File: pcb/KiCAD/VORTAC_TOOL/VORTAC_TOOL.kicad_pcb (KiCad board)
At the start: 4 copper layers, 18.2 x 7.6 mm, 6 parts, among them J1 Conn_01x05, J2 Conn_01x02, J3 Conn_01x03

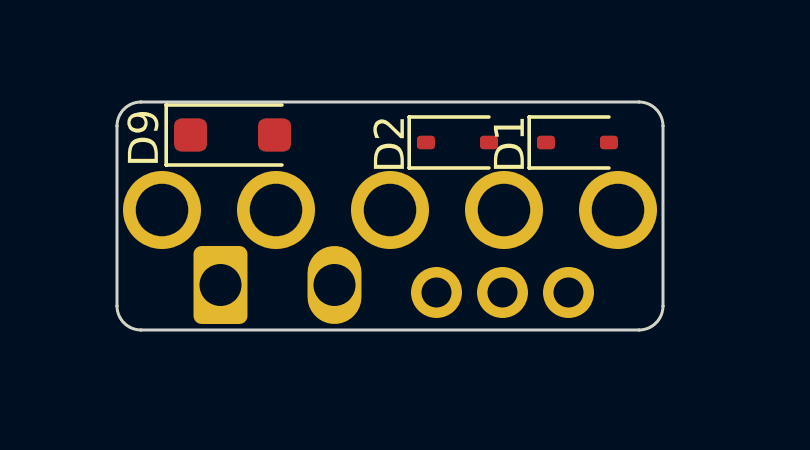
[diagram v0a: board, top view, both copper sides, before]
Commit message: updateting Custom Foorprints to show Ref**
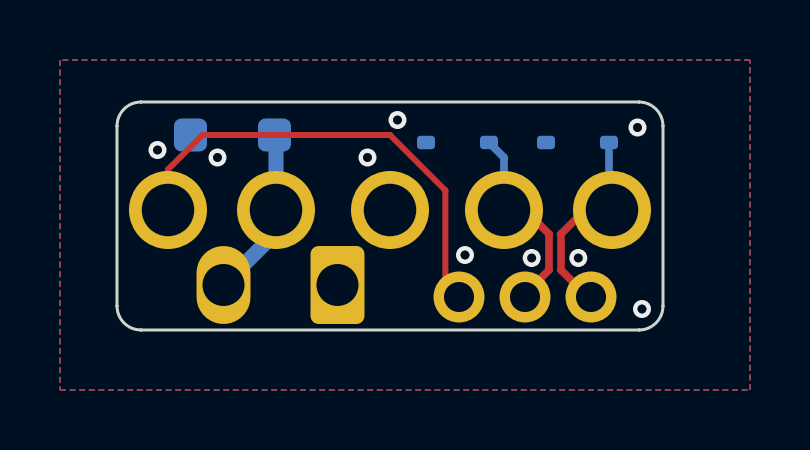
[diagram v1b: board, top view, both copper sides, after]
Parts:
- D1, D2, J1, J2, J3: moved to B.Cu
- D3: renamed from D9; moved to B.Cu
- moved J1 7.60 mm to (101.0, 52.0), turned to 0 degrees
- moved J2 3.90 mm to (99.2, 54.5)
- moved J3 0.76 mm to (103.3, 54.9), turned to -90 degrees
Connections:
- J1 pad 1: VDC -> TOOL_ID
- J1 pad 2: TOOL_ID -> VDC
- J1 pad 4: CAN_H -> CAN_L
- J1 pad 5: CAN_L -> CAN_H
- J3 pad 2: CAN_H -> CAN_L
- J3 pad 3: CAN_L -> CAN_H
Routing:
- net TOOL_ID: track 0.00 -> 15.5 mm
- net CAN_H: track 0.00 -> 6.80 mm
- net CAN_L: track 0.00 -> 6.76 mm
- net VDC: track 0.00 -> 5.75 mm
- net GND: track 0.00 -> 0.75 mm, vias 0 -> 9
- added copper zone on B.Cu, net GND
- added copper zone on F.Cu, net GND
- added copper zone on In1.Cu, net VDC
- added copper zone on In2.Cu, net VDC

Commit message: Added VORTAC_TOOLPLATE_REV2
Modified VORTAC_TOOL
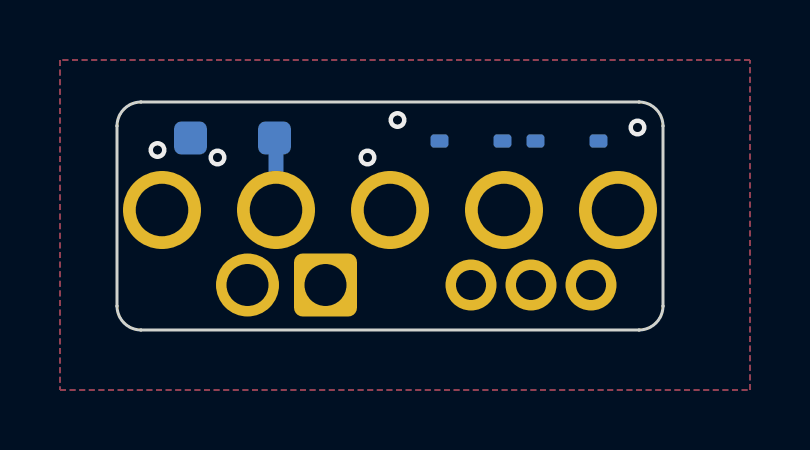
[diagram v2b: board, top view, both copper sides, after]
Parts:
- J3: footprint Vortac:Toolplate_Solderpoint_01x03_Data -> Vortac:Toolplate_Solderpoint_01x03_Data_Small
- moved J3 0.57 mm to (103.7, 54.5)
- moved D2 0.45 mm to (103.7, 49.7)
- moved J2 0.40 mm to (98.8, 54.5)
- moved D1 0.35 mm to (106.9, 49.7)
- moved D3 0.10 mm to (95.8, 49.6)
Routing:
- net TOOL_ID: track 15.5 -> 0.00 mm
- net CAN_H: track 6.80 -> 0.00 mm
- net CAN_L: track 6.76 -> 0.00 mm
- net VDC: track 5.75 -> 2.52 mm
- net GND: track 0.75 -> 0.00 mm, vias 9 -> 5
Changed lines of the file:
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@@
 	(footprint "Vortac:Toolplate_Solderpoint_01x02_Power_Small"
 		(layer "B.Cu")
-		(at 99.25 54.5 90)
+		(at 98.85 54.5 90)
 		(property "Reference" "J2"
 			(at 0 2.6 270)
@@
 		)
 		(pad "1" thru_hole roundrect
-			(at 0 0 90)
-			(size 2.6 1.8)
+			(at 0 0)
+			(size 2.1 2.1)
 			(drill 1.4)
 			(layers "*.Cu" "*.Mask")
 			(remove_unused_layers no)
-			(roundrect_rratio 0.15)
+			(roundrect_rratio 0.1388888889)
 			(net 3 "GND")
 			(pinfunction "Pin_1")
@@
 			(thermal_bridge_angle 0)
 		)
-		(pad "2" thru_hole oval
-			(at 0 -3.8 90)
-			(size 2.6 1.8)
+		(pad "2" thru_hole circle
+			(at 0 -2.6)
+			(size 2.1 2.1)
 			(drill 1.4)
 			(layers "*.Cu" "*.Mask")
@@
 		)
 		(pad "1" thru_hole circle
-			(at -7.4 0)
+			(at -7.6 0)
 			(size 2.6 2.6)
 			(drill 1.75)
@@
 		)
 		(pad "5" thru_hole circle
-			(at 7.4 0)
+			(at 7.6 0)
 			(size 2.6 2.6)
 			(drill 1.75)
@@
 		(embedded_fonts no)
 	)
-	(footprint "Vortac:Toolplate_Solderpoint_01x03_Data"
+	(footprint "Vortac:Toolplate_Solderpoint_01x03_Data_Small"
 		(layer "B.Cu")
-		(at 103.3 54.9 -90)
+		(at 103.7 54.5 -90)
 		(property "Reference" "J3"
 			(at 0.04 1.75 90)
@@
 		(attr smd exclude_from_bom)
 		(fp_text user "${REFERENCE}"
-			(at 0.25 -6.2 0)
+			(at -3.2 -2.6 0)
 			(unlocked yes)
 			(layer "B.Fab")
@@
 		)
 		(pad "2" thru_hole circle
-			(at 0 -2.2 270)
+			(at 0 -2 270)
 			(size 1.7 1.7)
 			(drill 1)
@@
 		)
 		(pad "3" thru_hole circle
-			(at 0 -4.4 270)
+			(at 0 -4 270)
 			(size 1.7 1.7)
 			(drill 1)
@@
 	(footprint "Diode_SMD:D_SOD-323"
 		(layer "B.Cu")
-		(at 103.25 49.75)
+		(at 103.7 49.7)
 		(descr "SOD-323")
 		(tags "SOD-323")
@@
 			(at -2.25 -0.05 90)
 			(layer "B.SilkS")
+			(hide yes)
 			(effects
 				(font
@@
 			(at 0.1 -1.9 180)
 			(layer "B.Fab")
+			(hide yes)
 			(effects
 				(font
@@
 	(footprint "Diode_SMD:D_SOD-123F"
 		(layer "B.Cu")
-		(at 95.75 49.5)
+		(at 95.75 49.6)
 		(descr "D_SOD-123F")
 		(tags "D_SOD-123F")
@@
 			(at -2.95 -0.1 90)
 			(layer "B.SilkS")
+			(hide yes)
 			(effects
 				(font
@@
 		)
 		(property "Value" "PTVS26VS1UR,115-ES"
-			(at 5.7 -3.5 180)
-			(layer "B.Fab")
+			(at 0.45 -3.55 180)
+			(layer "B.Fab")
+			(hide yes)
 			(effects
 				(font
@@
 	(footprint "Diode_SMD:D_SOD-323"
 		(layer "B.Cu")
-		(at 107.25 49.75)
+		(at 106.9 49.7)
 		(descr "SOD-323")
 		(tags "SOD-323")
@@
 			(at -2.25 -0.05 90)
 			(layer "B.SilkS")
+			(hide yes)
 			(effects
 				(font
@@
 			(at 0.1 -1.9 180)
 			(layer "B.Fab")
+			(hide yes)
 			(effects
 				(font
@@
 	)
 	(segment
-		(start 106.7 52.8)
-		(end 107.5 52)
-		(width 0.254)
-		(layer "F.Cu")
-		(net 1)
-	)
-	(segment
-		(start 106.7 54)
-		(end 106.7 52.8)
-		(width 0.254)
-		(layer "F.Cu")
-		(net 1)
-	)
-	(segment
-		(start 107.6 54.9)
-		(end 106.7 54)
-		(width 0.254)
-		(layer "F.Cu")
-		(net 1)
-	)
-	(segment
-		(start 107.5 52)
-		(end 108.4 52)
-		(width 0.254)
-		(layer "F.Cu")
-		(net 1)
-	)
-	(segment
-		(start 108.3 51.9)
-		(end 108.4 52)
-		(width 0.254)
-		(layer "B.Cu")
-		(net 1)
-	)
-	(segment
-		(start 108.3 49.75)
-		(end 108.3 51.9)
-		(width 0.254)
-		(layer "B.Cu")
-		(net 1)
-	)
-	(segment
-		(start 97.2 52.75)
-		(end 95.45 54.5)
-		(width 0.5)
-		(layer "B.Cu")
-		(net 2)
-	)
-	(segment
-		(start 97.2 52)
-		(end 97.2 52.75)
-		(width 0.5)
-		(layer "B.Cu")
-		(net 2)
-	)
-	(segment
 		(start 97.2 52)
 		(end 97.2 49.55)
@@
 	)
 	(via
-		(at 107.277 53.6)
-		(size 0.6)
-		(drill 0.3)
-		(layers "F.Cu" "B.Cu")
-		(free yes)
-		(net 3)
-	)
-	(via
 		(at 109.25 49.25)
 		(size 0.6)
@@
 	)
 	(via
-		(at 109.4 55.3)
-		(size 0.6)
-		(drill 0.3)
-		(layers "F.Cu" "B.Cu")
-		(free yes)
-		(net 3)
-	)
-	(via
-		(at 105.723 53.6)
-		(size 0.6)
-		(drill 0.3)
-		(layers "F.Cu" "B.Cu")
-		(free yes)
-		(net 3)
-	)
-	(via
-		(at 103.5 53.5)
-		(size 0.6)
-		(drill 0.3)
-		(layers "F.Cu" "B.Cu")
-		(free yes)
-		(net 3)
-	)
-	(via
 		(at 93.25 50)
 		(size 0.6)
@@
 		(net 3)
 	)
-	(segment
-		(start 99.25 53.75)
-		(end 99.25 54.5)
-		(width 0.3)
-		(layer "B.Cu")
-		(net 3)
-	)
-	(segment
-		(start 105.5 52)
-		(end 104.8 52)
-		(width 0.254)
-		(layer "F.Cu")
-		(net 4)
-	)
-	(segment
-		(start 105.4 54.9)
-		(end 106.3 54)
-		(width 0.254)
-		(layer "F.Cu")
-		(net 4)
-	)
-	(segment
-		(start 106.3 52.8)
-		(end 105.5 52)
-		(width 0.254)
-		(layer "F.Cu")
-		(net 4)
-	)
-	(segment
-		(start 106.3 54)
-		(end 106.3 52.8)
-		(width 0.254)
-		(layer "F.Cu")
-		(net 4)
-	)
-	(segment
-		(start 104.8 50.25)
-		(end 104.3 49.75)
-		(width 0.254)
-		(layer "B.Cu")
-		(net 4)
-	)
-	(segment
-		(start 104.8 52)
-		(end 104.8 50.25)
-		(width 0.254)
-		(layer "B.Cu")
-		(net 4)
-	)
-	(segment
-		(start 101 49.5)
-		(end 94.75 49.5)
-		(width 0.2)
-		(layer "F.Cu")
-		(net 5)
-	)
-	(segment
-		(start 103.2 54.9)
-		(end 102.846723 54.546723)
-		(width 0.2)
-		(layer "F.Cu")
-		(net 5)
-	)
-	(segment
-		(start 102.846723 54.546723)
-		(end 102.846723 51.346723)
-		(width 0.2)
-		(layer "F.Cu")
-		(net 5)
-	)
-	(segment
-		(start 102.846723 51.346723)
-		(end 101 49.5)
-		(width 0.2)
-		(layer "F.Cu")
-		(net 5)
-	)
-	(segment
-		(start 93.6 50.65)
-		(end 93.6 52)
-		(width 0.2)
-		(layer "F.Cu")
-		(net 5)
-	)
-	(segment
-		(start 94.75 49.5)
-		(end 93.6 50.65)
-		(width 0.2)
-		(layer "F.Cu")
-		(net 5)
-	)
 	(zone

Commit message: (Hopefully) Finalized DOCK, TOOL and TOOLPLATE REV2 for ordering
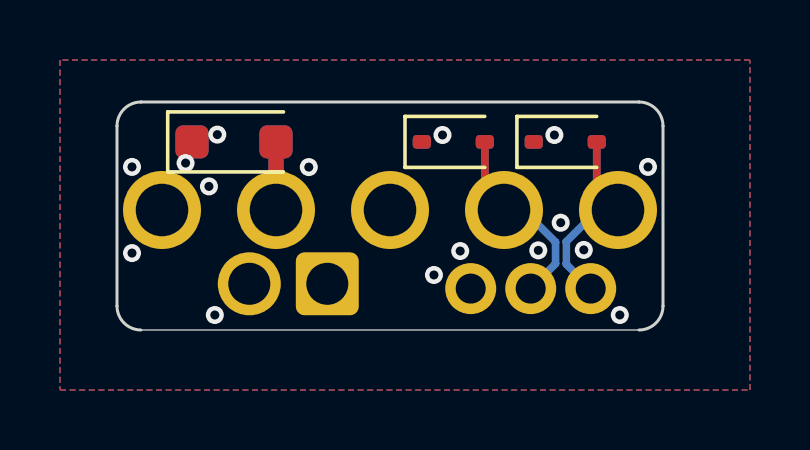
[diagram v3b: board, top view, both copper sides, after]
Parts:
- added D3: UDD32C24L01, Diode_SMD:D_SOD-323, F.Cu at (106.8, 49.7)
- added D4: UDD32C24L01, Diode_SMD:D_SOD-323, F.Cu at (103.1, 49.7)
- added D6: PTVS26VS1UR,115-ES, Diode_SMD:D_SOD-123F, F.Cu at (95.8, 49.7)
- moved D2 0.59 mm to (103.1, 49.7)
- moved D5 0.14 mm to (95.8, 49.7)
- moved J3 0.12 mm to (103.7, 54.6)
- moved J2 0.07 mm to (98.9, 54.5)
- moved D1 0.06 mm to (106.8, 49.7)
- renumbered D3 to D5
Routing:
- net TOOL_ID: track 0.00 -> 14.5 mm
- net CAN_H: track 0.00 -> 9.19 mm
- net CAN_L: track 0.00 -> 9.13 mm
- net VDC: track 2.52 -> 4.54 mm
- net GND: vias 5 -> 16
- added copper zone on In2.Cu, net GND
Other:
- board text added: "CH"
- board text added: "CL"
- board text added: "ID"
